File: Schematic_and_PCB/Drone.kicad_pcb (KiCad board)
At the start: 2 copper layers, 218.4 x 101.6 mm, 0 parts

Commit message: Schematic and PCB design
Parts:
- added C1: 1000uF, Capacitor_THT:CP_Radial_D7.5mm_P2.50mm, F.Cu at (114.3, 50.8)
- added C2: 100uF, Capacitor_THT:CP_Radial_D6.3mm_P2.50mm, F.Cu at (106.7, 43.1)
- added D1: 1N5822, Diode_THT:D_DO-201AD_P15.24mm_Horizontal, F.Cu at (96.5, 50.8)
- added D2: 1N5817, Diode_THT:D_DO-41_SOD81_P10.16mm_Horizontal, F.Cu at (27.9, 25.4)
- added D3: 1N5817, Diode_THT:D_DO-41_SOD81_P10.16mm_Horizontal, F.Cu at (116.8, 27.9)
- added D4: 1N5817, Diode_THT:D_DO-41_SOD81_P10.16mm_Horizontal, F.Cu at (116.8, 63.5)
- added D5: 1N5817, Diode_THT:D_DO-41_SOD81_P10.16mm_Horizontal, F.Cu at (33.0, 63.5)
- added ESP32: NodeMCU_DevKitC_v4, Module:NodeMCU DevKitC v4, B.Cu at (68.6, 55.9)
- added J1: BATT, Connector:JWT_A3963_1x02_P3.96mm_Vertical, F.Cu at (114.3, 43.2)
- added J2: PinHeader_1x10_P1.27mm_Vertical, Connector_PinHeader_1.27mm:PinHeader_1x10_P1.27mm_Vertical, F.Cu at (25.4, 48.3)
- added J5: Motor 4, Connector_PinHeader_1.00mm:PinHeader_1x02_P1.00mm_Vertical, F.Cu at (22.9, 22.9)
- added J6: Motor 1, Connector_PinHeader_1.00mm:PinHeader_1x02_P1.00mm_Vertical, F.Cu at (116.8, 22.9)
- added J7: Motor 2, Connector_PinHeader_1.00mm:PinHeader_1x02_P1.00mm_Vertical, F.Cu at (116.8, 68.6)
- added J8: Motor 3, Connector_PinHeader_1.00mm:PinHeader_1x02_P1.00mm_Vertical, F.Cu at (22.9, 68.6)
- added L1: 100uH 1A, Inductor_THT:L_Radial_D8.7mm_P5.00mm_Fastron_07HCP, F.Cu at (104.1, 48.3)
- added Q1: IRLZ34N, Package_TO_SOT_THT:TO-220-3_Vertical, F.Cu at (33.0, 68.6)
- added Q2: IRLZ34N, Package_TO_SOT_THT:TO-220-3_Vertical, F.Cu at (99.1, 63.5)
- added Q3: IRLZ34N, Package_TO_SOT_THT:TO-220-3_Vertical, F.Cu at (99.1, 22.9)
- added Q4: IRLZ34N, Package_TO_SOT_THT:TO-220-3_Vertical, F.Cu at (43.2, 25.4)
- added U1: LM2576HVS-3.3, Package_TO_SOT_SMD:TO-263-5_TabPin3, F.Cu at (90.4, 40.6)
- added U2: TC4424EPA, Package_DIP:DIP-8_W7.62mm_Socket, F.Cu at (48.2, 50.0)
- added U3: TC4424EPA, Package_DIP:DIP-8_W7.62mm_Socket, F.Cu at (61.0, 58.5)
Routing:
- net GND: track 0.00 -> 408.2 mm, vias 0 -> 2
- net Net-(D2-K): track 0.00 -> 334.9 mm, vias 0 -> 2
- net Net-(ESP32-Pin_1): track 0.00 -> 166.2 mm, vias 0 -> 1
- net Net-(Q4-G): track 0.00 -> 65.2 mm
- net Net-(Q3-G): track 0.00 -> 58.7 mm
- net (no net): track 0.00 -> 49.1 mm
- net Net-(Q2-G): track 0.00 -> 43.3 mm, vias 0 -> 1
- net Net-(D2-A): track 0.00 -> 25.5 mm
- net Net-(D4-A): track 0.00 -> 22.9 mm
- net Net-(Q1-G): track 0.00 -> 22.9 mm
- net Net-(D3-A): track 0.00 -> 20.8 mm
- net Net-(D5-A): track 0.00 -> 19.7 mm
- net Net-(D1-K): track 0.00 -> 18.7 mm, vias 0 -> 1
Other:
- board size 218.4 x 101.6 mm -> 100 x 50 mm

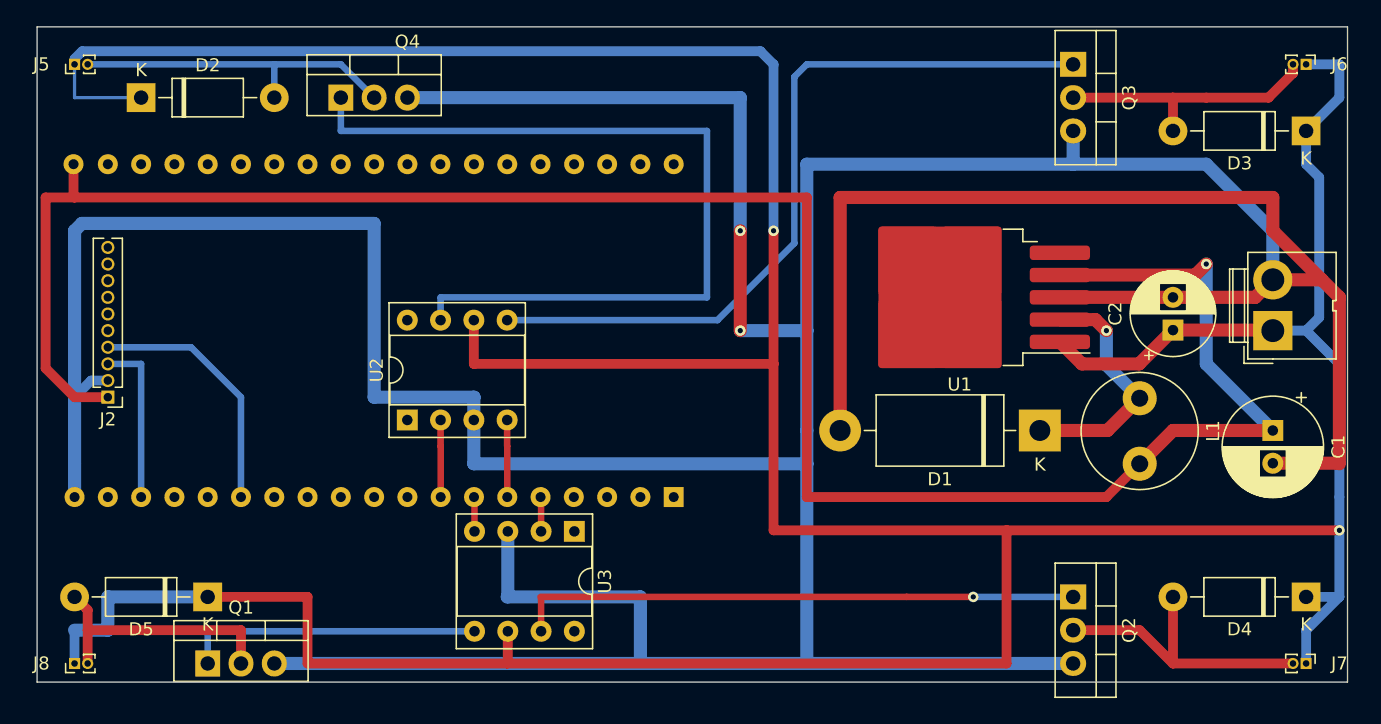
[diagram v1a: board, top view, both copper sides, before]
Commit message: Bugfix in pcb for aliexpress ESP32
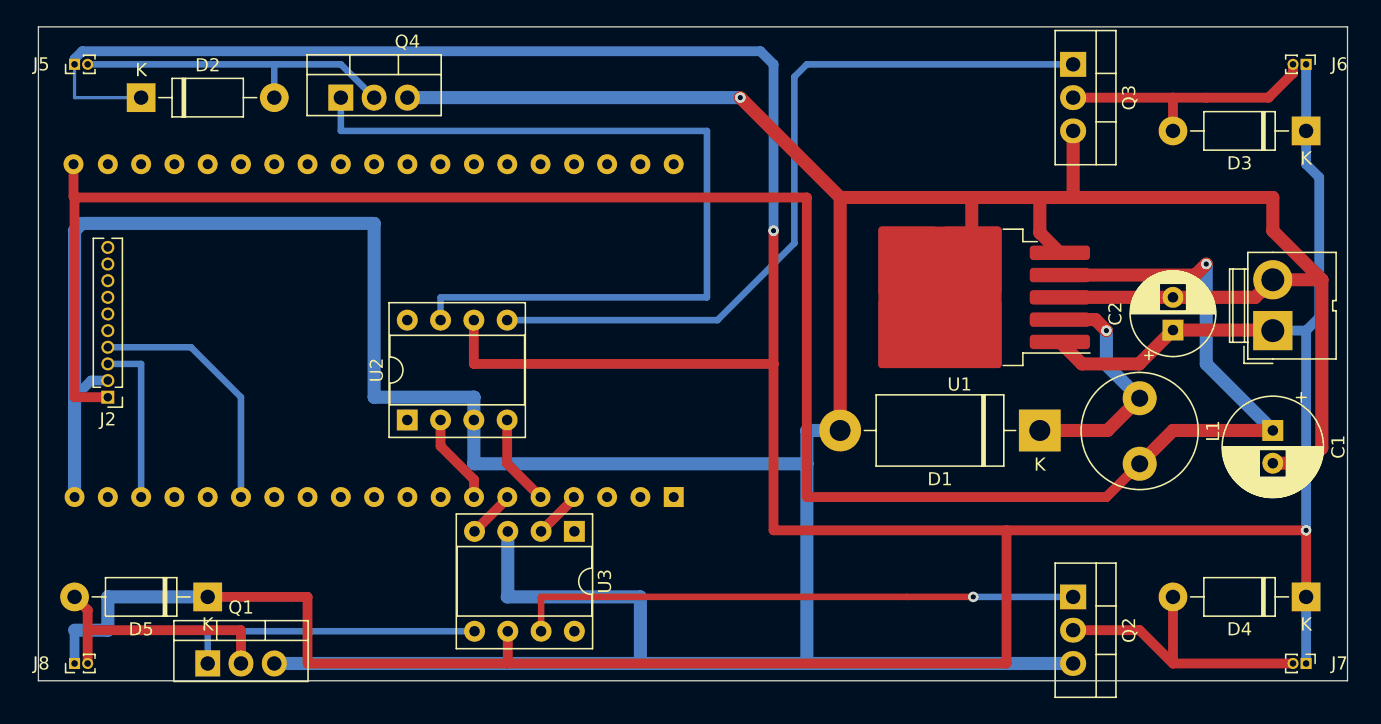
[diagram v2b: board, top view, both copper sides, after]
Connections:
- C1 pad 2: (no net) -> GND
- U1 pad 5: unconnected-(U1-~{ON}/OFF-Pad5) -> GND
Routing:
- net GND: track 408.2 -> 346.7 mm, vias 2 -> 1
- net Net-(D2-K): track 334.9 -> 324.1 mm
- net (no net): track 49.1 -> 53.4 mm
- net Net-(ESP32-Pin_1): track 166.2 -> 163.1 mm
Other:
- board size 100 x 50 mm -> 99.9 x 49.9 mm

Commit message: Schematic Update for better fitting
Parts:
- removed J2: PinHeader_1x10_P1.27mm_Vertical, Connector_PinHeader_1.27mm:PinHeader_1x10_P1.27mm_Vertical
- added ?: , , F.Cu at (30.5, 38.1)
- added ?: , , F.Cu at (30.5, 43.2)
- added ?: , , F.Cu at (30.5, 40.6)
- added ?: , , F.Cu at (30.5, 35.6)
- moved ESP32 5.08 mm to (73.7, 55.9)
- moved J8 2.61 mm to (25.4, 68.0), turned to -90 degrees
- moved J5 2.54 mm to (22.9, 25.4), turned to 180 degrees
- moved Q2 2.54 mm to (99.1, 61.0)
- moved J7 1.00 mm to (116.8, 67.6)
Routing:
- net Net-(ESP32-Pin_1): track 163.1 -> 142.8 mm
- net Net-(D2-K): track 324.1 -> 313.0 mm
- net Net-(Q4-G): track 65.2 -> 74.8 mm
- net GND: track 346.7 -> 352.3 mm
- net Net-(D2-A): track 25.5 -> 30.7 mm
- net Net-(D4-A): track 22.9 -> 20.3 mm
- net Net-(Q2-G): track 43.3 -> 45.8 mm
- net Net-(D3-A): track 20.8 -> 18.4 mm
